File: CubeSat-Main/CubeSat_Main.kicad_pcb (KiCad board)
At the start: 2 copper layers, 92 x 92 mm, 25 parts, among them J1 Conn_01x03_Pin, J2 Conn_01x08_Socket, J3 Conn_01x03_Pin, U1 STM32F411CEU6 - BlackPill, U2 LORA E220-900T22D, U3 BNO055, U4 GPS_NEO6M, U5 LM7805_TO220, U6 LM35-LP

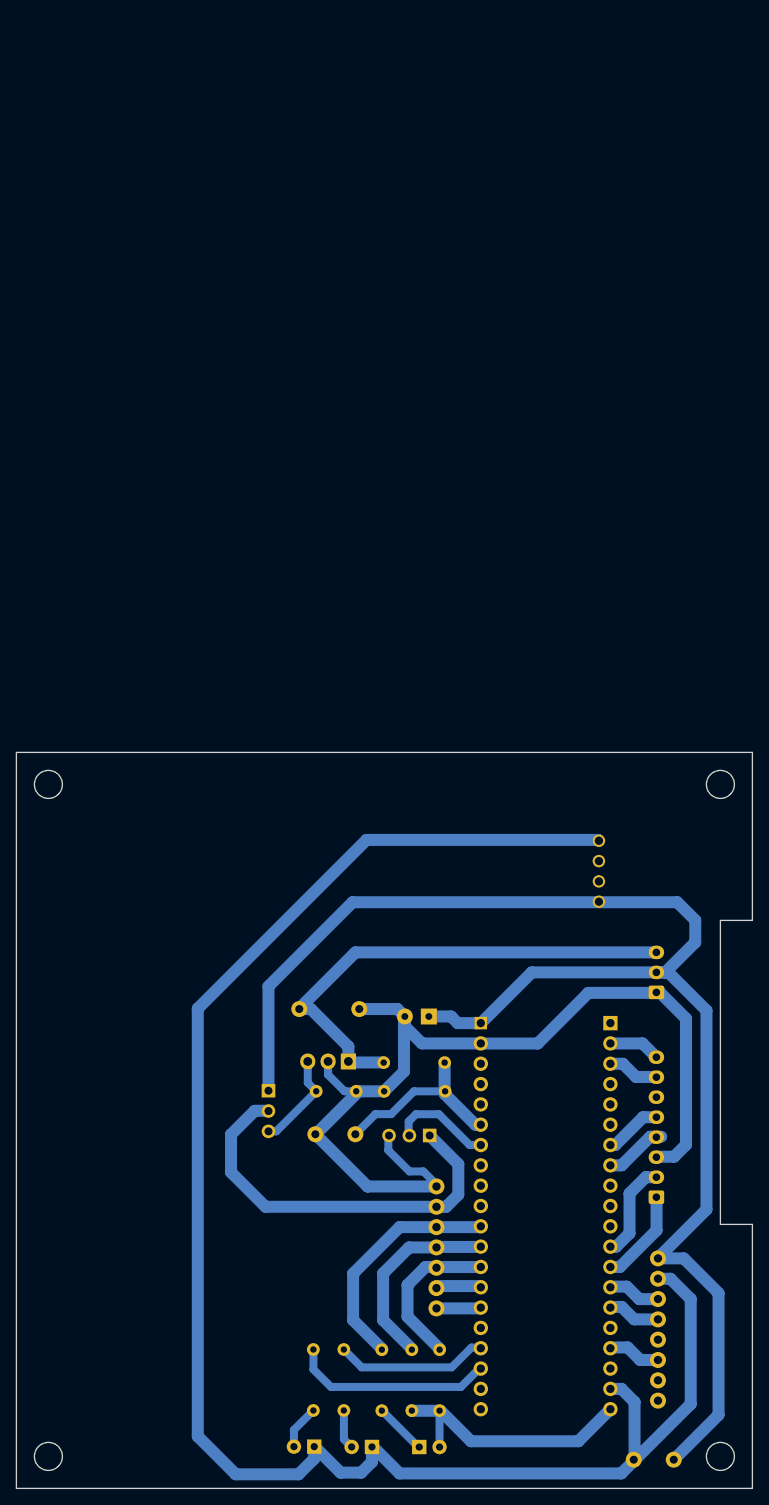
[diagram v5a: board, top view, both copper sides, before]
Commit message: final changes in ALL 3 pcbs: mounting wholes config, and a few connector changes
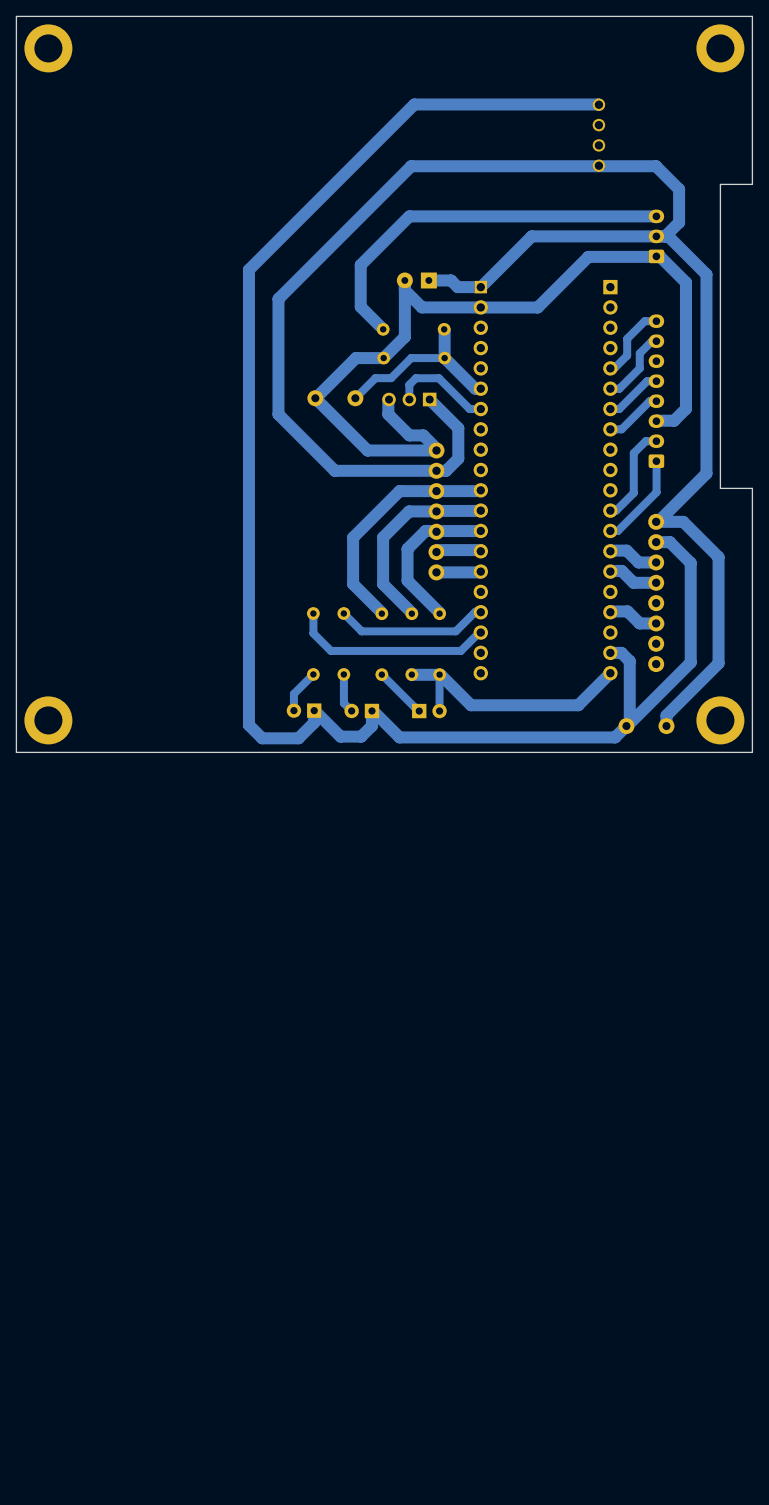
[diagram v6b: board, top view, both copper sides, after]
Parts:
- removed C4: 0.33uF, Capacitor_THT:C_Disc_D8.0mm_W5.0mm_P7.50mm
- removed C5: 0.1uF, Capacitor_THT:C_Disc_D8.0mm_W2.5mm_P5.00mm
- removed J3: Conn_01x03_Pin, Connector_PinHeader_2.54mm:PinHeader_1x03_P2.54mm_Vertical
- removed U5: LM7805_TO220, Package_TO_SOT_THT:TO-220-3_Vertical
- added REF**: MountingHole_3.5mm_Pad, MountingHole:MountingHole_3.5mm_Pad, B.Cu at (4.00, -4.00)
- added REF**: MountingHole_3.5mm_Pad, MountingHole:MountingHole_3.5mm_Pad, B.Cu at (88.0, -4.00)
- added REF**: MountingHole_3.5mm_Pad, MountingHole:MountingHole_3.5mm_Pad, B.Cu at (4.00, -88.0)
- added REF**: MountingHole_3.5mm_Pad, MountingHole:MountingHole_3.5mm_Pad, B.Cu at (88.0, -88.0)
- moved U3 92.1 mm to (84.5, -19.9)
- moved C1 92.0 mm to (50.1, -59.0)
- moved C3 92.0 mm to (37.4, -44.3)
- moved D1 92.0 mm to (50.4, -5.17)
- moved D2 92.0 mm to (44.4, -5.18)
- moved D3 92.0 mm to (37.2, -5.22)
- moved G*** 92.0 mm to (22.4, -88.6)
- moved J1 92.0 mm to (80.0, -62.0)
- moved J2 92.0 mm to (80.0, -36.4)
- moved R1 92.0 mm to (52.9, -17.3)
- moved R2 92.0 mm to (49.4, -17.3)
- moved R3 92.0 mm to (45.7, -17.3)
- moved R4 92.0 mm to (40.9, -17.4)
- moved R5 92.0 mm to (37.1, -17.4)
- moved U1 92.0 mm to (66.2, -33.7)
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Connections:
- U1 pad 26: M1_PWM1 -> unconnected-(U1-PB13-Pad26)
- U1 pad 27: M1_PWM2 -> unconnected-(U1-PB14-Pad27)
- U1 pad 29: unconnected-(U1-PA8-Pad29) -> M1_PWM1
- U1 pad 30: unconnected-(U1-PA9-Pad30) -> M1_PWM2
- U2 pad 6: 5V_E220 -> VIN_5V
- U4 pad 2: unconnected-(U4-RX-Pad2) -> GPS_RX
- U4 pad 3: unconnected-(U4-TX-Pad3) -> GPS_TX
- U6 pad 1: 5V_E220 -> VIN_5V
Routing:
- net 5V_E220: track 50.3 -> 0.00 mm
- net VIN_5V: track 185.9 -> 220.9 mm
- net GND: track 339.6 -> 316.9 mm
- net Vbat_8.4V: track 62.0 -> 48.7 mm
- net 5V_LDO: track 12.2 -> 0.00 mm
- net M1_PWM2: track 6.45 -> 9.52 mm
- net M1_PWM1: track 6.52 -> 9.50 mm
- net M2_PWM2: track 7.84 -> 7.21 mm
- net Vbat_ADC: track 23.9 -> 23.3 mm
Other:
- outline, holes or cut-outs redrawn
- board text removed: "BUCK"
- board text removed: "LDO"

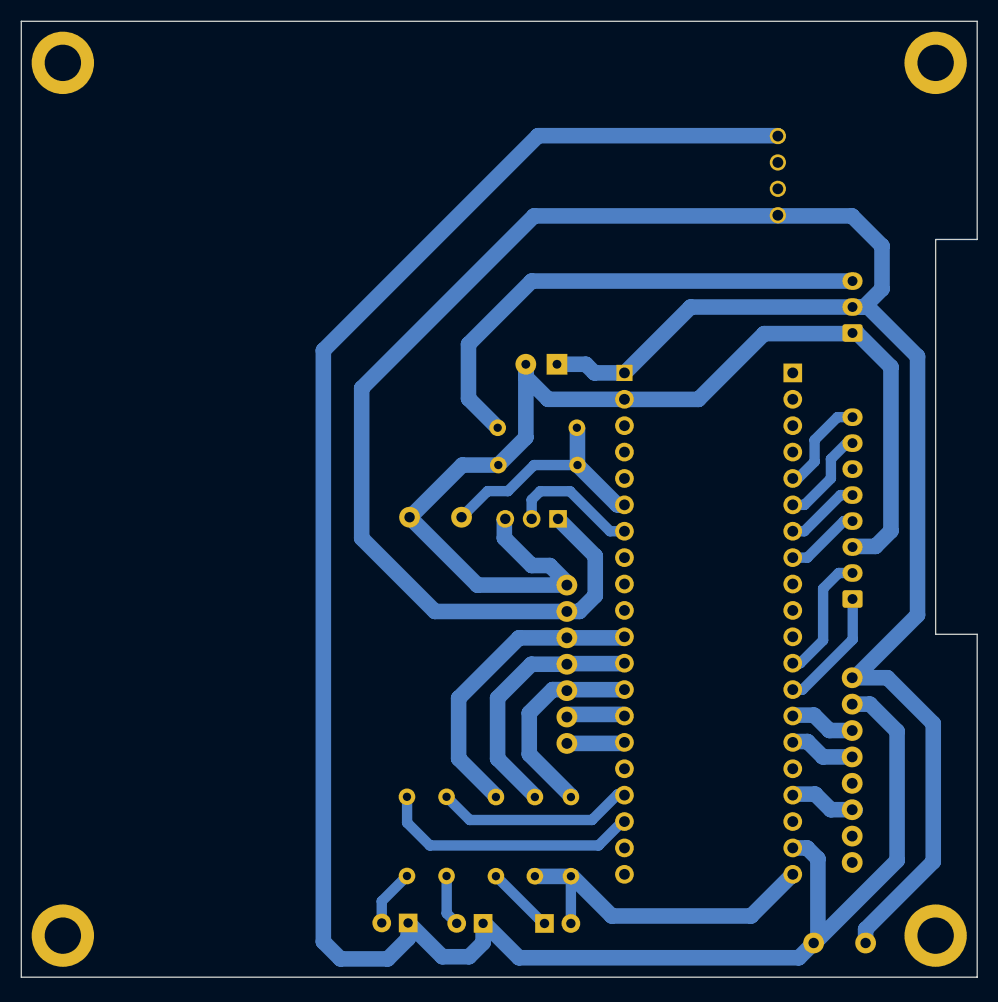
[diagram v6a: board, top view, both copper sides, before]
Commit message: changing the size of the vias
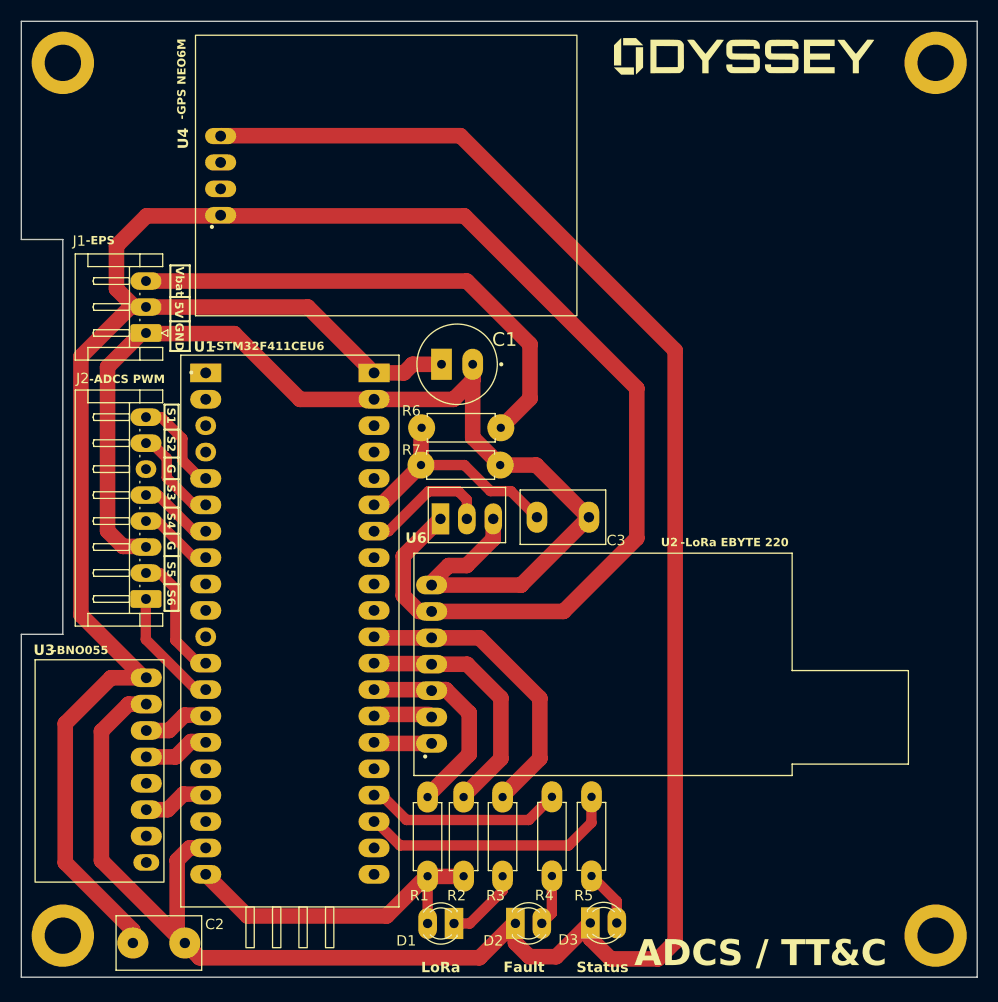
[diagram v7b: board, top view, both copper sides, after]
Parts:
- C1, C2, C3, D1, D2, D3, G***, J1, J2, R1, R2, R3, R4, R5, R6, R7, REF** (x4), U1, U2, U3, U4, U6: moved to F.Cu
- moved REF** 84.0 mm to (88.0, -4.00), turned to 0 degrees
- moved REF** 84.0 mm to (4.00, -4.00), turned to 0 degrees
- moved REF** 84.0 mm to (88.0, -88.0), turned to 0 degrees
- moved REF** 84.0 mm to (4.00, -88.0), turned to 0 degrees
- moved U3 76.9 mm to (7.53, -19.9), turned to 0 degrees
- moved J1 68.0 mm to (12.0, -62.0)
- moved J2 68.0 mm to (12.0, -36.4)
- moved C2 60.5 mm to (15.7, -3.29), turned to 180 degrees
- moved G*** 47.3 mm to (69.6, -88.6), turned to 0 degrees
- moved U1 40.3 mm to (25.9, -33.7), turned to 0 degrees
- moved U4 22.7 mm to (34.7, -77.3)
- moved U2 20.0 mm to (56.0, -30.1)
- moved R5 17.8 mm to (54.9, -17.4)
- moved D3 17.5 mm to (54.8, -5.22), turned to 0 degrees
- moved C3 17.3 mm to (54.6, -44.3), turned to 180 degrees
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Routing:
- net Net-(D1-K): track 6.61 -> 7.43 mm
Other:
- outline, holes or cut-outs redrawn

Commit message: new Main and EPS PCBs, all previous problems corrected, final version
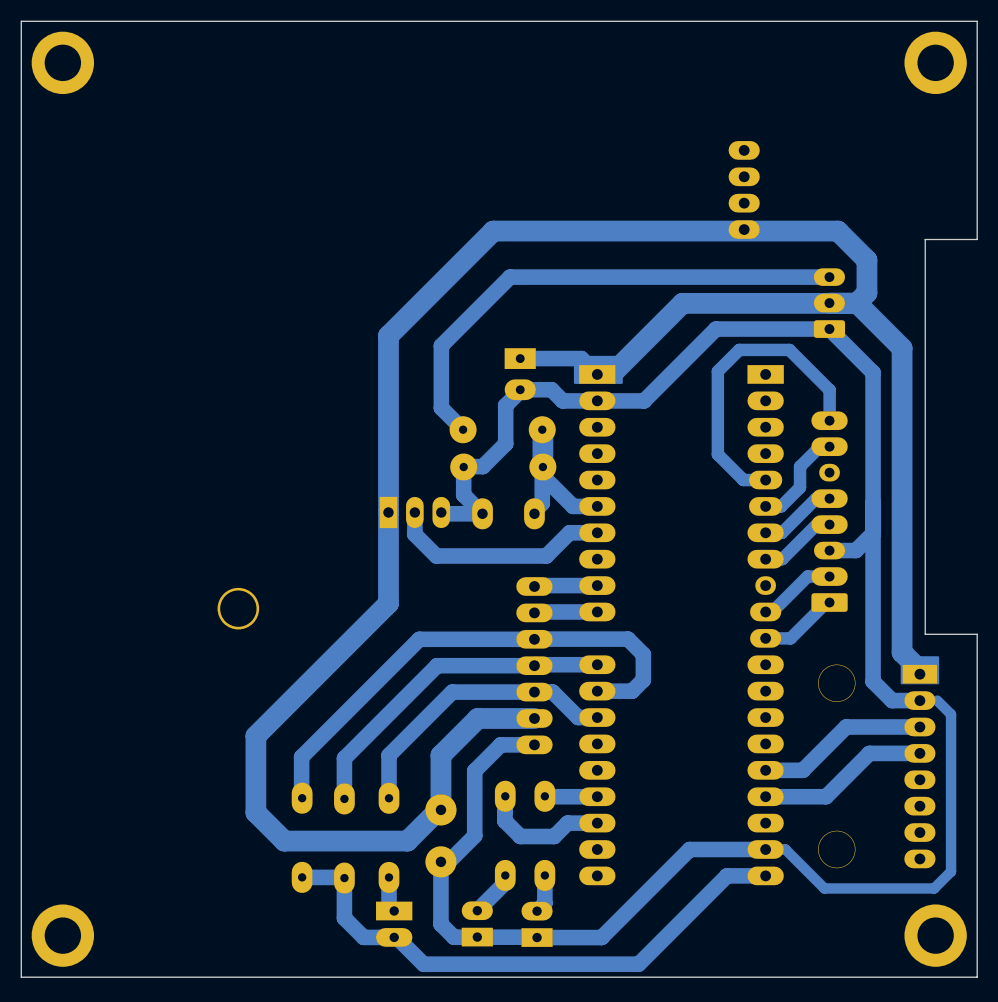
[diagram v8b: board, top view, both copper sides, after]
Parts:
- C1, C2, C3, D1, D2, D3, G***, J1, J2, R2, R4, R5, R6, R7, REF** (x4), U1, U2, U3, U4, U6: moved to B.Cu
- R1: renamed from R3; moved to B.Cu
- R3: renamed from R1; moved to B.Cu
- moved REF** 84.0 mm to (4.00, -4.00), turned to 180 degrees
- moved REF** 84.0 mm to (88.0, -4.00), turned to 180 degrees
- moved REF** 84.0 mm to (4.00, -88.0), turned to 180 degrees
- moved REF** 84.0 mm to (88.0, -88.0), turned to 180 degrees
- moved U3 74.5 mm to (82.0, -20.3)
- moved J2 65.8 mm to (77.8, -36.1)
- moved J1 65.8 mm to (77.8, -62.4)
- moved G*** 48.1 mm to (21.5, -88.6), turned to 180 degrees
- moved U1 37.7 mm to (63.5, -33.5), turned to 180 degrees
- moved C2 25.9 mm to (40.4, -11.1), turned to 90 degrees
- moved U2 23.1 mm to (32.9, -30.0)
- moved U4 19.5 mm to (54.1, -75.9)
- moved R3 12.1 mm to (27.0, -17.2)
- moved R7 11.7 mm to (50.2, -49.1), turned to 180 degrees
- moved R2 11.5 mm to (31.1, -17.2)
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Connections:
- U1 pad 10: E220_M0 -> unconnected-(U1-PA0-Pad10)
- U1 pad 11: E220_M1 -> E220_AUX
- U1 pad 15: unconnected-(U1-PA5-Pad15) -> E220_M1
- U1 pad 16: unconnected-(U1-PA6-Pad16) -> E220_M0
- U1 pad 38: unconnected-(U1-PA15-Pad38) -> M3_PWM1
- U1 pad 39: unconnected-(U1-PB3-Pad39) -> M3_PWM2
- U1 pad 40: M3_PWM1 -> unconnected-(U1-PB4-Pad40)
- U1 pad 41: M3_PWM2 -> unconnected-(U1-PB5-Pad41)
- U1 pad 42: BNO055_SCL -> GPS_RX
- U1 pad 43: BNO055_SDA -> GPS_TX
- U1 pad 45: unconnected-(U1-PB8-Pad45) -> BNO055_SCL
- U1 pad 46: BNO055_INT -> BNO055_SDA
- U3 pad 6: BNO055_INT -> unconnected-(U3-INT-Pad6)
- U4 pad 2: GPS_RX -> unconnected-(U4-RX-Pad2)
- U4 pad 3: GPS_TX -> unconnected-(U4-TX-Pad3)
- U4 pad 4: GND -> unconnected-(U4-GND-Pad4)
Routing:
- net GND: track 317.0 -> 198.2 mm
- net E220_RX: track 19.8 -> 49.5 mm
- net STM_3.3V: track 32.9 -> 53.9 mm
- net M1_PWM1: track 9.50 -> 30.4 mm
- net LED_RED: track 19.1 -> 5.65 mm
- net LED_BLUE: track 25.3 -> 12.4 mm
- net BNO055_SDA: track 6.24 -> 16.6 mm
- net BNO055_SCL: track 6.24 -> 16.6 mm
- net Temp_ADC: track 12.7 -> 21.5 mm
- net Vbat_ADC: track 23.3 -> 16.1 mm
- net E220_TX: track 25.0 -> 31.8 mm
- net BNO055_INT: track 6.38 -> 0.00 mm
- net M3_PWM1: track 12.3 -> 7.56 mm
- net M3_PWM2: track 11.8 -> 7.58 mm
- net Net-(D1-K): track 7.43 -> 3.44 mm
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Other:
- outline, holes or cut-outs redrawn
- board text added: "-LM35DZ"
- board text added: "ADCS/TT&C"
- board text removed: "ADCS / TT&C"
